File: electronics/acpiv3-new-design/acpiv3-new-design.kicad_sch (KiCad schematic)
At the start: 0 parts

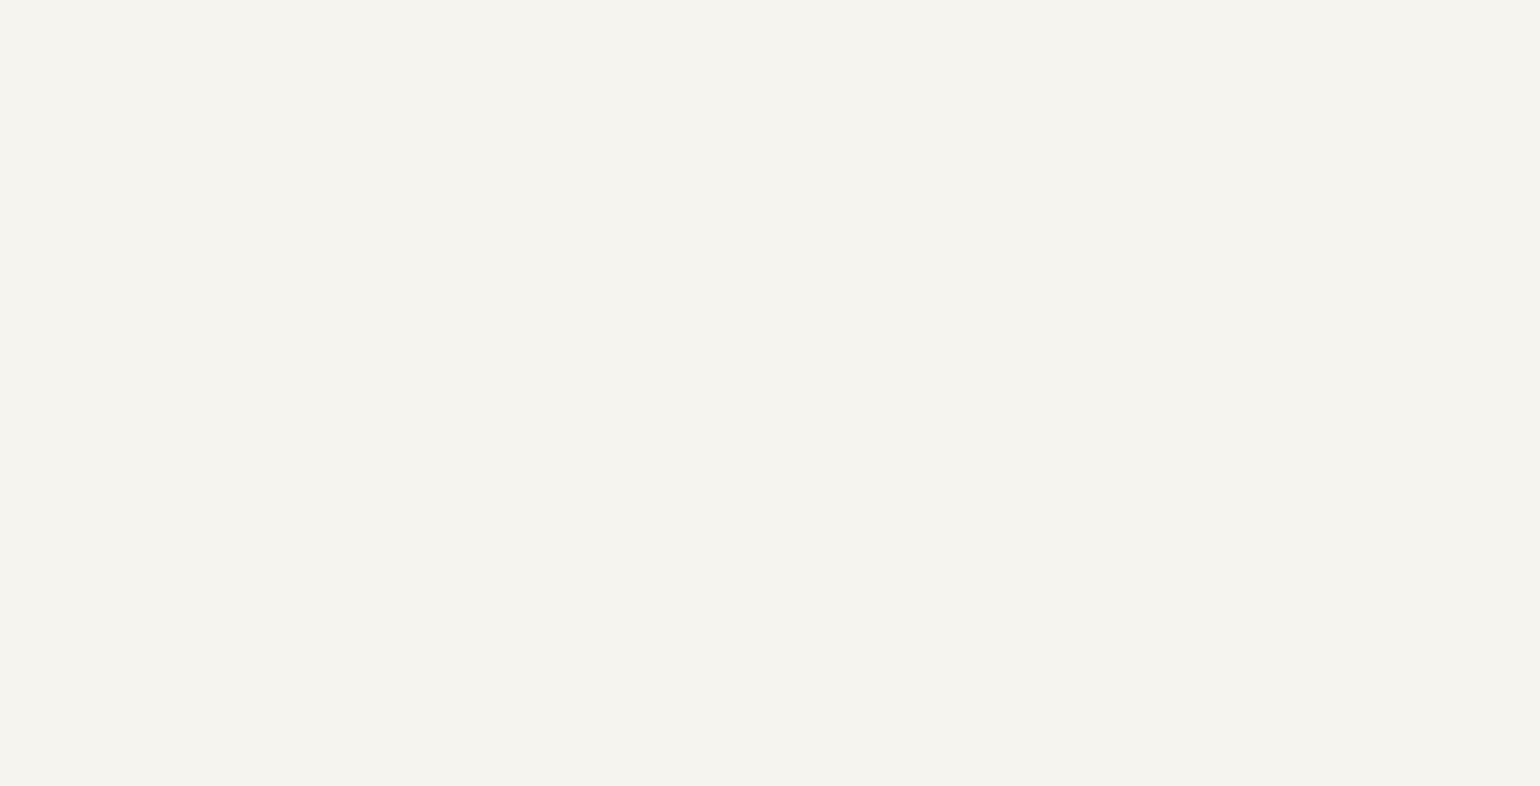
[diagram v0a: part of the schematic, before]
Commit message: fix(electronics): corregir drivers de motor y limpiar seguimiento de git
Los dos canales de vibracion estaban mal cableados: el motor colgaba entre
colector y emisor sin llegar nunca a la bateria, el emisor no iba a tierra y
el diodo de flyback quedaba en serie en el retorno y en directa.

Topologia corregida en ambos canales:
- motor entre +BATT y el colector del PN2222A
- diodo en paralelo con el motor, catodo a +BATT (bloquea en operacion normal)
- emisor a GND, unificado con el negativo de la bateria y la tierra de U1/U2
- base via resistencia a GPIO4 (canal 1) y GPIO10 (canal 2)

El canal 2 pasa de GPIO20 a GPIO10: GPIO20 es U0RXD y habria peleado con la
consola serie del ESP32-C3.

Limpieza de git: .history de KiCad habia quedado registrado como gitlink sin
.gitmodules, lo que rompia el clonado. Se deja de rastrear junto con los
archivos .lck y se anaden las reglas correspondientes a .gitignore.

Pendiente: huellas de D1, D2, J1, J2 y J3; valores de resistencias y diodos;
condensador de bulk en +BATT; y revisar la alimentacion, porque la LiPo de
3.7 V esta cableada al pin 5V, que es el VBUS del USB.

Co-Authored-By: Claude Opus 5 <noreply@anthropic.com>
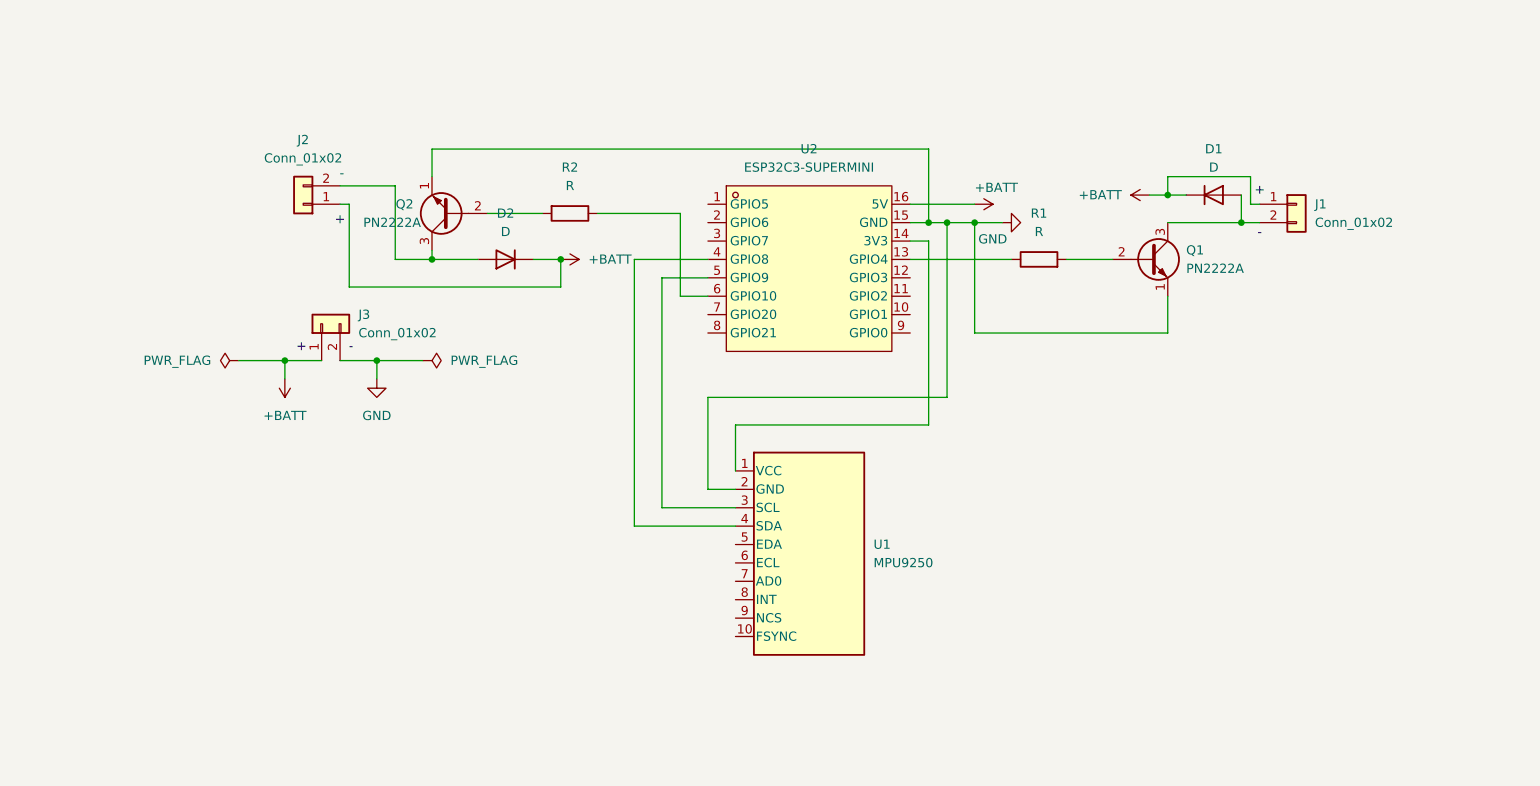
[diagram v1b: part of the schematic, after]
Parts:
- added D1, D2: D, symbol Device:D
- added J1, J2, J3: Conn_01x02, symbol Connector_Generic:Conn_01x02
- added Q1, Q2: PN2222A, Package_TO_SOT_THT:TO-92_Inline, symbol Transistor_BJT:PN2222A
- added R1, R2: R, symbol Device:R
- added U1: MPU9250, acpi-modulos:MPU9250_1x10_P2.54mm_THT, symbol acpi-modulos:MPU9250
- added U2: ESP32C3-SUPERMINI, acpi-modulos:COMM-SMD_16P-L22.5-W18.0-P2.54-TL, symbol acpi-modulos:ESP32C3-SUPERMINI
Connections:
- new net: U1.1 (VCC), U2.14 (3V3)
- new net: U1.3 (SCL), U2.5 (GPIO9)
- new net: U1.4 (SDA), U2.4 (GPIO8)
- new net: Q1.2 (B), R1.2
- new net: D1.2 (A), J1.2 (Pin_2), Q1.3 (C)
- new net: D2.2 (A), J2.2 (Pin_2), Q2.3 (C)
- new net: R1.1, U2.13 (GPIO4)
- new net: Q2.2 (B), R2.2
- new net: R2.1, U2.6 (GPIO10)
- new net +BATT: D1.1 (K), D2.1 (K), J1.1 (Pin_1), J2.1 (Pin_1), J3.1 (Pin_1), U2.16 (5V)
- new net GND: J3.2 (Pin_2), Q1.1 (E), Q2.1 (E), U1.2 (GND), U2.15 (GND)
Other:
- note added: "+"
- note added: "-"
